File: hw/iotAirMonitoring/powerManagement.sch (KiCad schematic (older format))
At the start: 29 parts, among them J1 USB_C_Receptacle_USB2.0, Q3 2N7002

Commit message: Finish stepdown schematic
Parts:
- removed R? (x2): R, symbol Device:R
- added J2: USB_DATA, Connector_PinHeader_2.54mm:PinHeader_1x02_P2.54mm_Vertical, symbol Connector_Generic:Conn_01x02
- C1, C2: footprint (none) -> Capacitor_SMD:C_0805_2012Metric; LCSC (none) -> C45783
- C10: renamed from C?; value C -> 47p; footprint (none) -> Capacitor_SMD:C_0402_1005Metric; LCSC (none) -> C1567
- C11: renamed from C?; value C -> 10n; footprint (none) -> Capacitor_SMD:C_0402_1005Metric; LCSC (none) -> C15195
- C3: renamed from C?; value 100n -> 100n/16V; footprint (none) -> Capacitor_SMD:C_0402_1005Metric; LCSC (none) -> C1525
- C4, C5: renamed from C?; value 47u -> 47u/6V3; footprint (none) -> Capacitor_SMD:C_0805_2012Metric; LCSC (none) -> C16780
- C6, C7: renamed from C?; value C -> 4u7/16V; footprint (none) -> Capacitor_SMD:C_0603_1608Metric; LCSC (none) -> C19666
- C8: renamed from C?; value C -> 10n/50V; footprint (none) -> Capacitor_SMD:C_0402_1005Metric; LCSC (none) -> C15195
- C9: renamed from C?; value C -> 1n; footprint (none) -> Capacitor_SMD:C_0402_1005Metric; LCSC (none) -> C1523
- D1: renamed from D?; value D_Schottky -> SS54; footprint (none) -> Diode_SMD:D_SMA; LCSC (none) -> C22452
- J1: symbol Connector:USB_C_Receptacle_USB2.0 -> iotAirMonitoring-rescue:USB_C_Receptacle_USB2.0-Connector
- L1: renamed from L?; value L -> 4u7; footprint (none) -> Inductor_SMD:L_Bourns-SRN6028
- R1, R2: footprint (none) -> Resistor_SMD:R_0402_1005Metric; LCSC (none) -> C25905
- R3, R4, R5: footprint (none) -> Resistor_SMD:R_0402_1005Metric; LCSC (none) -> C25741
- R6: footprint (none) -> Resistor_SMD:R_0402_1005Metric; LCSC (none) -> C25744
- R7: renamed from R?; value R -> 15k; footprint (none) -> Resistor_SMD:R_0402_1005Metric; LCSC (none) -> C25756
- R8: renamed from R?; value R -> 4k7; footprint (none) -> Resistor_SMD:R_0402_1005Metric; LCSC (none) -> C25900
- R9: renamed from R?; value R -> 30k; footprint (none) -> Resistor_SMD:R_0603_1608Metric; LCSC (none) -> C22984
- gave numbers to parts that had none: 3
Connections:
- no-connect marks 2 -> 3
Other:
- note added: "R_down=(R_up*Vref)/(Vout-Vref)"
- note added: "SLOW START\n10nF -> 4ms"
- moved on the sheet: C3, C5, C6, C8, R7, R8

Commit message: Add LDO regulator and ESP32
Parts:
- added C12, C13: 22u, Capacitor_SMD:C_0805_2012Metric, symbol Device:C
- added U2: AMS1117-3.3, Package_TO_SOT_SMD:SOT-223-3_TabPin2, symbol Regulator_Linear:AMS1117-3.3
- J1: symbol iotAirMonitoring-rescue:USB_C_Receptacle_USB2.0-Connector -> iotAirMonitoring-rescue:USB_C_Receptacle_USB2.0-Connector-iotAirMonitoring-rescue
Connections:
- net labels added: 3V3_L
- wire segments 103 -> 115
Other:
- note added: "3V3 LDO FOR ANALOG SENSORS"
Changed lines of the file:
@@
 $EndDescr
 $Comp
-L iotAirMonitoring-rescue:USB_C_Receptacle_USB2.0-Connector J1
+L iotAirMonitoring-rescue:USB_C_Receptacle_USB2.0-Connector-iotAirMonitoring-rescue J1
 U 1 1 617675BE
 P 1500 2000
@@
 	2150 2100 2350 2100
 Connection ~ 2150 2100
+$Comp
+L Regulator_Linear:AMS1117-3.3 U2
+U 1 1 6177D292
+P 8800 4100
+F 0 "U2" H 8800 4342 50  0000 C CNN
+F 1 "AMS1117-3.3" H 8800 4251 50  0000 C CNN
+F 2 "Package_TO_SOT_SMD:SOT-223-3_TabPin2" H 8800 4300 50  0001 C CNN
+F 3 "http://www.advanced-monolithic.com/pdf/ds1117.pdf" H 8900 3850 50  0001 C CNN
+F 4 "C6186" H 8800 4100 50  0001 C CNN "LCSC"
+	1    8800 4100
+	1    0    0    -1
+$EndComp
+$Comp
+L Device:C C13
+U 1 1 6177EB7E
+P 9200 4350
+F 0 "C13" H 9315 4396 50  0000 L CNN
+F 1 "22u" H 9315 4305 50  0000 L CNN
+F 2 "Capacitor_SMD:C_0805_2012Metric" H 9238 4200 50  0001 C CNN
+F 3 "~" H 9200 4350 50  0001 C CNN
+F 4 "C45783" H 9200 4350 50  0001 C CNN "LCSC"
+	1    9200 4350
+	1    0    0    -1
+$EndComp
+Wire Wire Line
+	9100 4100 9200 4100
+Wire Wire Line
+	9200 4100 9200 4200
+Wire Wire Line
+	9200 4100 9300 4100
+Connection ~ 9200 4100
+Text HLabel 9300 4100 2    50   Output ~ 0
+3V3_L
+Text HLabel 8800 4700 3    50   UnSpc ~ 0
+GND
+Wire Wire Line
+	8800 4400 8800 4550
+Wire Wire Line
+	8800 4550 9200 4550
+Wire Wire Line
+	9200 4550 9200 4500
+Connection ~ 8800 4550
+Wire Wire Line
+	8800 4550 8800 4700
+$Comp
+L Device:C C12
+U 1 1 6178E735
+P 8300 4350
+F 0 "C12" H 8415 4396 50  0000 L CNN
+F 1 "22u" H 8415 4305 50  0000 L CNN
+F 2 "Capacitor_SMD:C_0805_2012Metric" H 8338 4200 50  0001 C CNN
+F 3 "~" H 8300 4350 50  0001 C CNN
+F 4 "C45783" H 8300 4350 50  0001 C CNN "LCSC"
+	1    8300 4350
+	1    0    0    -1
+$EndComp
+Wire Wire Line
+	8300 4200 8300 4100
+Wire Wire Line
+	8300 4100 8500 4100
+Wire Wire Line
+	8300 4500 8300 4550
+Wire Wire Line
+	8300 4550 8800 4550
+Wire Wire Line
+	8300 4100 8200 4100
+Connection ~ 8300 4100
+Text HLabel 8200 4100 0    50   Output ~ 0
+VDD
+Text Notes 8200 3750 0    50   ~ 0
+3V3 LDO FOR ANALOG SENSORS
 $EndSCHEMATC

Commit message: Add way more parts to schematic
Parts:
- added Q5: 2N7002, Package_TO_SOT_SMD:SOT-23, symbol Transistor_FET:2N7002
- added Q6: AO3400A, Package_TO_SOT_SMD:SOT-23, symbol Device:Q_NMOS_GSD
- added R19: 10k, Resistor_SMD:R_0402_1005Metric, symbol Device:R
- J1: symbol iotAirMonitoring-rescue:USB_C_Receptacle_USB2.0-Connector-iotAirMonitoring-rescue -> iotAirMonitoring-rescue:USB_C_Receptacle_USB2.0-Connector-iotAirMonitoring-rescue-iotAirMonitoring-rescue
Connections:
- net labels added: LDO_EN
- wire segments 115 -> 120
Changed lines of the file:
@@
 $EndDescr
 $Comp
-L iotAirMonitoring-rescue:USB_C_Receptacle_USB2.0-Connector-iotAirMonitoring-rescue J1
+L iotAirMonitoring-rescue:USB_C_Receptacle_USB2.0-Connector-iotAirMonitoring-rescue-iotAirMonitoring-rescue J1
 U 1 1 617675BE
 P 1500 2000
@@
 Wire Wire Line
 	8300 4550 8800 4550
-Wire Wire Line
-	8300 4100 8200 4100
 Connection ~ 8300 4100
-Text HLabel 8200 4100 0    50   Output ~ 0
+Text HLabel 7450 4100 0    50   Output ~ 0
 VDD
 Text Notes 8200 3750 0    50   ~ 0
 3V3 LDO FOR ANALOG SENSORS
+$Comp
+L Transistor_FET:2N7002 Q5
+U 1 1 618169C2
+P 4600 1350
+F 0 "Q5" H 4805 1396 50  0000 L CNN
+F 1 "2N7002" H 4805 1305 50  0000 L CNN
+F 2 "Package_TO_SOT_SMD:SOT-23" H 4800 1275 50  0001 L CIN
+F 3 "https://www.fairchildsemi.com/datasheets/2N/2N7002.pdf" H 4600 1350 50  0001 L CNN
+	1    4600 1350
+	-1   0    0    -1
+$EndComp
+Connection ~ 4800 1350
+$Comp
+L Device:Q_NMOS_GSD Q6
+U 1 1 618707CD
+P 7700 4200
+F 0 "Q6" V 8042 4200 50  0000 C CNN
+F 1 "AO3400A" V 7951 4200 50  0000 C CNN
+F 2 "Package_TO_SOT_SMD:SOT-23" H 7900 4300 50  0001 C CNN
+F 3 "https://datasheet.lcsc.com/lcsc/1811081213_Alpha-&-Omega-Semicon-AO3400A_C20917.pdf" H 7700 4200 50  0001 C CNN
+F 4 "C20917" V 7700 4200 50  0001 C CNN "LCSC"
+	1    7700 4200
+	0    -1   -1   0
+$EndComp
+Text HLabel 7750 4450 2    50   Input ~ 0
+LDO_EN
+Wire Wire Line
+	7700 4400 7700 4450
+Wire Wire Line
+	7700 4450 7750 4450
+Wire Wire Line
+	7450 4100 7500 4100
+Wire Wire Line
+	7900 4100 8300 4100
+$Comp
+L Device:R R19
+U 1 1 618898DE
+P 7700 4650
+F 0 "R19" H 7770 4696 50  0000 L CNN
+F 1 "10k" H 7770 4605 50  0000 L CNN
+F 2 "Resistor_SMD:R_0402_1005Metric" V 7630 4650 50  0001 C CNN
+F 3 "~" H 7700 4650 50  0001 C CNN
+F 4 "C25744" H 7700 4650 50  0001 C CNN "LCSC"
+	1    7700 4650
+	1    0    0    -1
+$EndComp
+Wire Wire Line
+	7700 4500 7700 4450
+Connection ~ 7700 4450
+Text HLabel 7700 4850 3    50   UnSpc ~ 0
+GND
+Wire Wire Line
+	7700 4800 7700 4850
 $EndSCHEMATC

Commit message: Schematic nearly finished
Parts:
- removed Q5: 2N7002, Package_TO_SOT_SMD:SOT-23, symbol Transistor_FET:2N7002
- removed Q6: AO3400A, Package_TO_SOT_SMD:SOT-23, symbol Device:Q_NMOS_GSD
- removed R19: 10k, Resistor_SMD:R_0402_1005Metric, symbol Device:R
- added J11: PWR, Connector_PinHeader_2.54mm:PinHeader_1x02_P2.54mm_Vertical, symbol Connector_Generic:Conn_01x02
- added J12: USB_B_Micro, Connector_USB:USB_Micro-B_Amphenol_10118194_Horizontal, symbol Connector:USB_B_Micro
- added Q12: AO3401A, Package_TO_SOT_SMD:SOT-23, symbol Device:Q_PMOS_GSD
- added Q13: 2N7002, Package_TO_SOT_SMD:SOT-23, symbol Transistor_FET:2N7002
- added R33, R36: 100k, Resistor_SMD:R_0402_1005Metric, symbol Device:R
- J9: renamed from J1; footprint (none) -> Connector_USB:USB_C_Receptacle_HRO_TYPE-C-31-M-12
- renumbered C2 to C10, C3 to C11, C4 to C12, C5 to C13, C12 to C14, C13 to C15, C6 to C16, C7 to C17, C8 to C18, C9 to C19, C10 to C20, C11 to C21, C1 to C9, D1 to D5, J2 to J10, Q2 to Q10, Q3 to Q11, Q1 to Q9, R1 to R27, R2 to R28, R3 to R29, R4 to R30, R6 to R31, R5 to R32, R7 to R34, R8 to R35, R9 to R37, U2 to U3, U1 to U4
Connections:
- net labels added: D+, D-, USB_VDD
- net labels removed: USB_C_VDD
- wire segments 120 -> 138
- no-connect marks 3 -> 4
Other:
- moved on the sheet: J10, J9, R27, R28

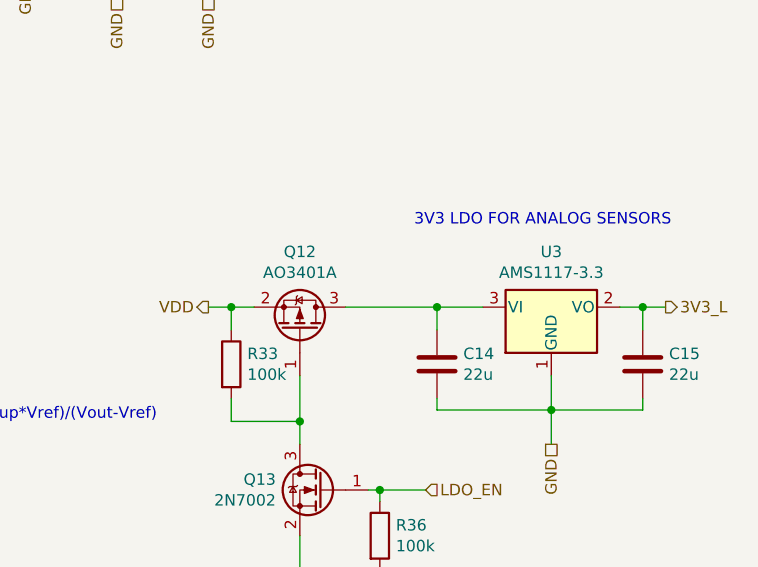
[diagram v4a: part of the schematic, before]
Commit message: Nearly finished schematic, add optional LoRa module
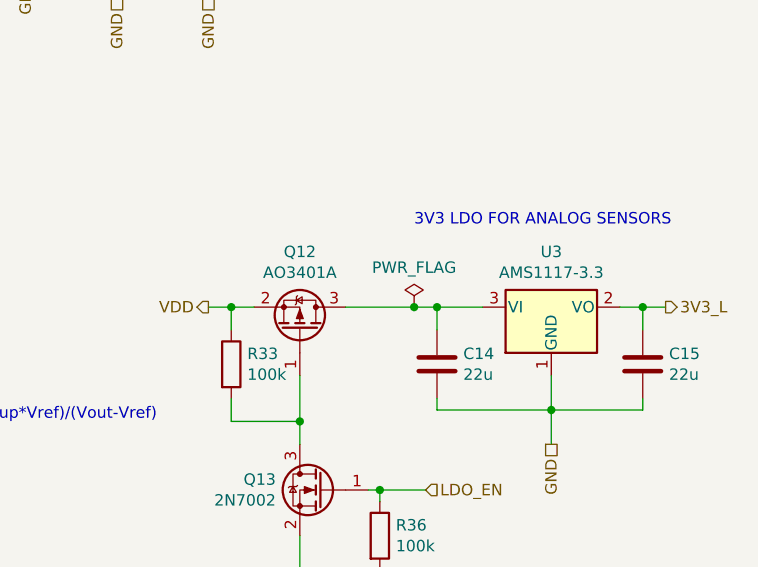
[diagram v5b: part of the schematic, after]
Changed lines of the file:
@@
 $Descr A4 11693 8268
 encoding utf-8
-Sheet 2 2
+Sheet 2 3
 Title ""
 Date ""
@@
 	7300 4100 7400 4100
 Wire Wire Line
-	7900 4100 8300 4100
+	7900 4100 8200 4100
 $Comp
 L power:PWR_FLAG #FLG01
@@
 Wire Wire Line
 	1900 1000 2050 1000
+$Comp
+L power:PWR_FLAG #FLG0102
+U 1 1 6188BF27
+P 8200 4100
+F 0 "#FLG0102" H 8200 4175 50  0001 C CNN
+F 1 "PWR_FLAG" H 8200 4273 50  0000 C CNN
+F 2 "" H 8200 4100 50  0001 C CNN
+F 3 "~" H 8200 4100 50  0001 C CNN
+	1    8200 4100
+	1    0    0    -1
+$EndComp
+Connection ~ 8200 4100
+Wire Wire Line
+	8200 4100 8300 4100
 $EndSCHEMATC

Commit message: Start routing of main board
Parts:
- J12: symbol Connector:USB_B_Micro -> iotAirMonitoring-rescue:USB_B_Micro-Connector
- J9: symbol iotAirMonitoring-rescue:USB_C_Receptacle_USB2.0-Connector-iotAirMonitoring-rescue-iotAirMonitoring-rescue -> iotAirMonitoring-rescue:USB_C_Receptacle_USB2.0-Connector-iotAirMonitoring-rescue-iotAirMonitoring-rescue-iotAirMonitor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
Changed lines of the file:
@@
 $EndDescr
 $Comp
-L iotAirMonitoring-rescue:USB_C_Receptacle_USB2.0-Connector-iotAirMonitoring-rescue-iotAirMonitoring-rescue J?
+L iotAirMonitoring-rescue:USB_C_Receptacle_USB2.0-Connector-iotAirMonitoring-rescue-iotAirMonitoring-rescue-iotAirMonitoring-rescue J?
 U 1 1 617675BE
 P 1300 1600
@@
 Connection ~ 8050 4900
 $Comp
-L Connector:USB_B_Micro J12
+L iotAirMonitoring-rescue:USB_B_Micro-Connector J12
 U 1 1 617FE196
 P 1050 3450
+AR Path="/617FE196" Ref="J12"  Part="1"
+AR Path="/61767442/617FE196" Ref="J12"  Part="1"
 F 0 "J12" H 1107 3917 50  0000 C CNN
 F 1 "USB_B_Micro" H 1107 3826 50  0000 C CNN

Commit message: More routing on main board
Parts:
- J12: symbol iotAirMonitoring-rescue:USB_B_Micro-Connector -> iotAirMonitoring-rescue:USB_B_Micro-Connector-iotAirMonitoring-rescue
- J9: symbol iotAirMonitoring-rescue:USB_C_Receptacle_USB2.0-Connector-iotAirMonitoring-rescue-iotAirMonitoring-rescue-iotAirMonitoring-rescue -> iotAirMonitoring-rescue:USB_C_Receptacle_USB2.0-Connector-iotAirMonitoring-rescue-iotAirMonitoring-rescue-iotAirMonitoring-rescue-iotAirMonitoring-rescue
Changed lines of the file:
@@
 encoding utf-8
 Sheet 2 3
-Title ""
+Title "iotAirMonitoring"
 Date ""
-Rev ""
+Rev "v0.1"
 Comp ""
 Comment1 ""
@@
 $EndDescr
 $Comp
-L iotAirMonitoring-rescue:USB_C_Receptacle_USB2.0-Connector-iotAirMonitoring-rescue-iotAirMonitoring-rescue-iotAirMonitoring-rescue J?
+L iotAirMonitoring-rescue:USB_C_Receptacle_USB2.0-Connector-iotAirMonitoring-rescue-iotAirMonitoring-rescue-iotAirMonitoring-rescue-iotAirMonitoring-rescue J?
 U 1 1 617675BE
 P 1300 1600
@@
 Connection ~ 8050 4900
 $Comp
-L iotAirMonitoring-rescue:USB_B_Micro-Connector J12
+L iotAirMonitoring-rescue:USB_B_Micro-Connector-iotAirMonitoring-rescue J12
 U 1 1 617FE196
 P 1050 3450

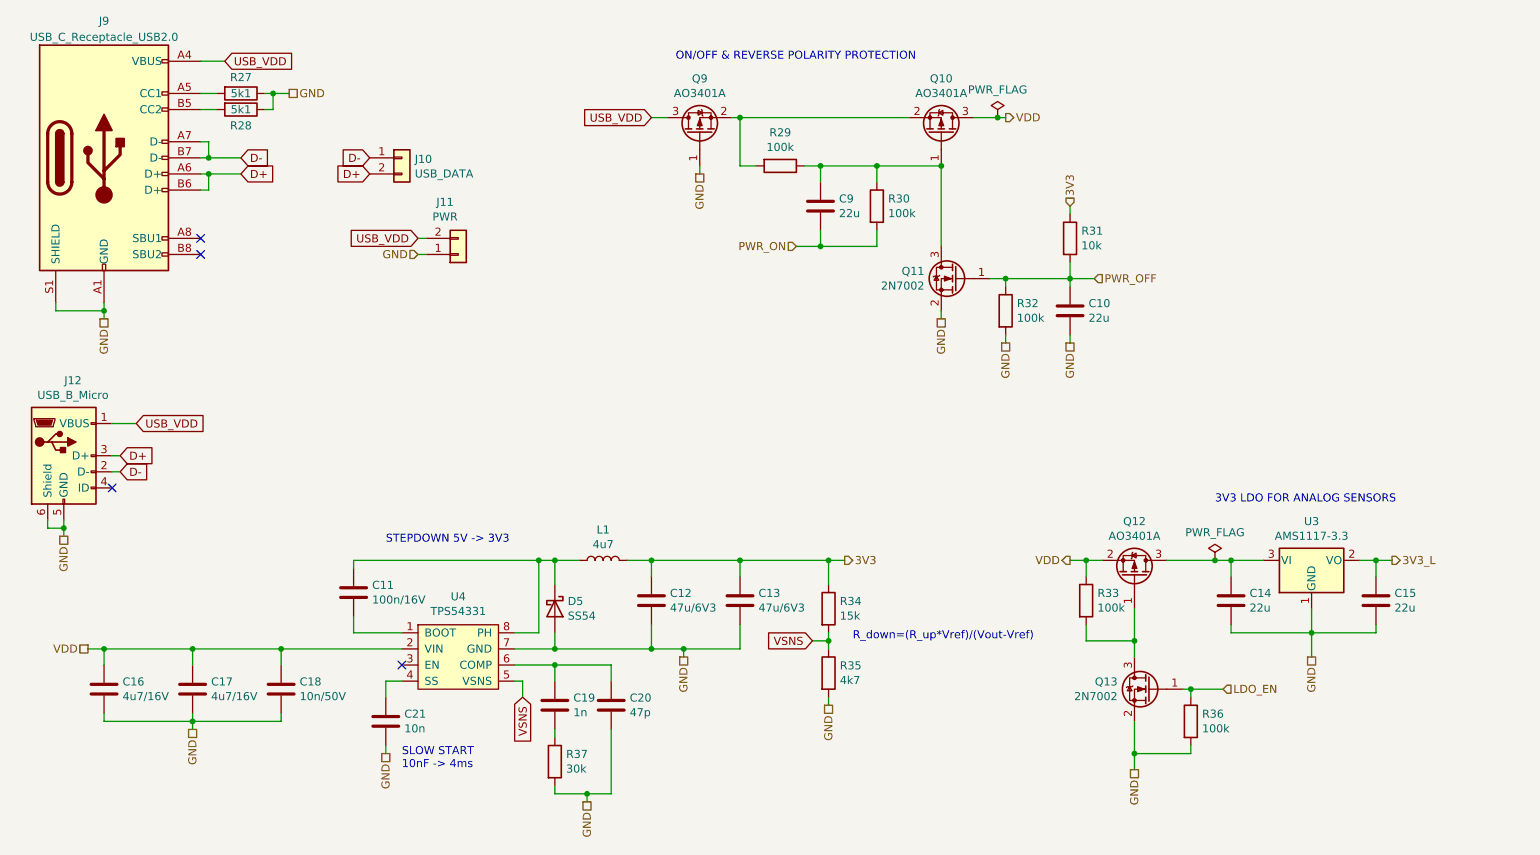
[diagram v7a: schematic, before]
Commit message: First version routed main board
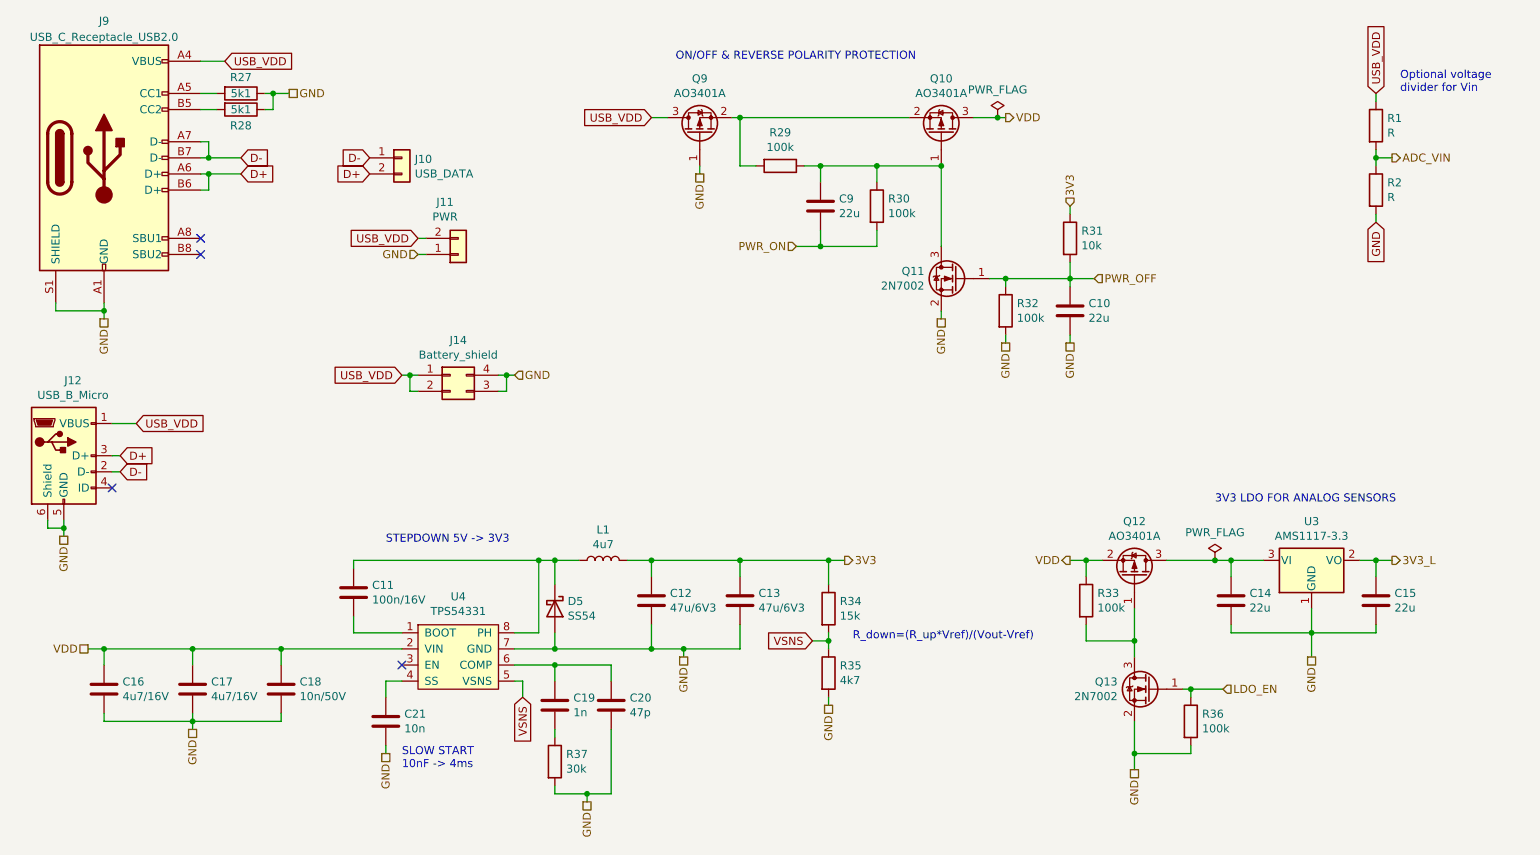
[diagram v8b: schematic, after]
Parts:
- added J14: Battery_shield, Connector_PinHeader_2.54mm:PinHeader_2x02_P2.54mm_Vertical, symbol Connector_Generic:Conn_02x02_Counter_Clockwise
- added R1, R2: R, Resistor_SMD:R_0805_2012Metric_Pad1.20x1.40mm_HandSolder, symbol Device:R
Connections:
- net GND: now also J14.3 (Pin_3), J14.4 (Pin_4), R2.2
- net USB_VDD: now also J14.1 (Pin_1), J14.2 (Pin_2), R1.1
- new net ADC_VIN: R1.2, R2.1
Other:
- note added: "Optional voltage\ndivider for Vin"
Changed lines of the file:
@@
 $Descr A4 11693 8268
 encoding utf-8
-Sheet 2 3
+Sheet 3 3
 Title "iotAirMonitoring"
 Date ""
@@
 Wire Wire Line
 	8200 4100 8300 4100
+$Comp
+L Connector_Generic:Conn_02x02_Counter_Clockwise J14
+U 1 1 6182A26C
+P 3450 2950
+F 0 "J14" H 3500 3167 50  0000 C CNN
+F 1 "Battery_shield" H 3500 3076 50  0000 C CNN
+F 2 "Connector_PinHeader_2.54mm:PinHeader_2x02_P2.54mm_Vertical" H 3450 2950 50  0001 C CNN
+F 3 "~" H 3450 2950 50  0001 C CNN
+	1    3450 2950
+	1    0    0    -1
+$EndComp
+Wire Wire Line
+	3250 2950 3200 2950
+Wire Wire Line
+	3200 2950 3200 3050
+Wire Wire Line
+	3200 3050 3250 3050
+Wire Wire Line
+	3750 2950 3800 2950
+Wire Wire Line
+	3800 2950 3800 3050
+Wire Wire Line
+	3800 3050 3750 3050
+Text GLabel 3150 2950 0    50   Input ~ 0
+USB_VDD
+Wire Wire Line
+	3150 2950 3200 2950
+Connection ~ 3200 2950
+Text HLabel 3850 2950 2    50   Input ~ 0
+GND
+Wire Wire Line
+	3800 2950 3850 2950
+Connection ~ 3800 2950
+$Comp
+L Device:R R?
+U 1 1 6188824F
+P 9200 1400
+AR Path="/6188824F" Ref="R?"  Part="1"
+AR Path="/61767442/6188824F" Ref="R1"  Part="1"
+F 0 "R1" H 9270 1446 50  0000 L CNN
+F 1 "R" H 9270 1355 50  0000 L CNN
+F 2 "Resistor_SMD:R_0805_2012Metric_Pad1.20x1.40mm_HandSolder" V 9130 1400 50  0001 C CNN
+F 3 "~" H 9200 1400 50  0001 C CNN
+	1    9200 1400
+	1    0    0    -1
+$EndComp
+$Comp
+L Device:R R?
+U 1 1 61888255
+P 9200 1800
+AR Path="/61888255" Ref="R?"  Part="1"
+AR Path="/61767442/61888255" Ref="R2"  Part="1"
+F 0 "R2" H 9270 1846 50  0000 L CNN
+F 1 "R" H 9270 1755 50  0000 L CNN
+F 2 "Resistor_SMD:R_0805_2012Metric_Pad1.20x1.40mm_HandSolder" V 9130 1800 50  0001 C CNN
+F 3 "~" H 9200 1800 50  0001 C CNN
+	1    9200 1800
+	1    0    0    -1
+$EndComp
+Wire Wire Line
+	9200 1550 9200 1600
+Wire Wire Line
+	9200 1600 9300 1600
+Connection ~ 9200 1600
+Wire Wire Line
+	9200 1600 9200 1650
+Wire Wire Line
+	9200 1250 9200 1200
+Wire Wire Line
+	9200 1950 9200 2000
+Text Notes 9350 1200 0    50   ~ 0
+Optional voltage\ndivider for Vin
+Text GLabel 9200 1200 1    50   Input ~ 0
+USB_VDD
+Text GLabel 9200 2000 3    50   Input ~ 0
+GND
+Text HLabel 9300 1600 2    50   Output ~ 0
+ADC_VIN
 $EndSCHEMATC
